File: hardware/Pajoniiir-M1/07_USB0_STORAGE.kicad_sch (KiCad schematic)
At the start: 7 parts

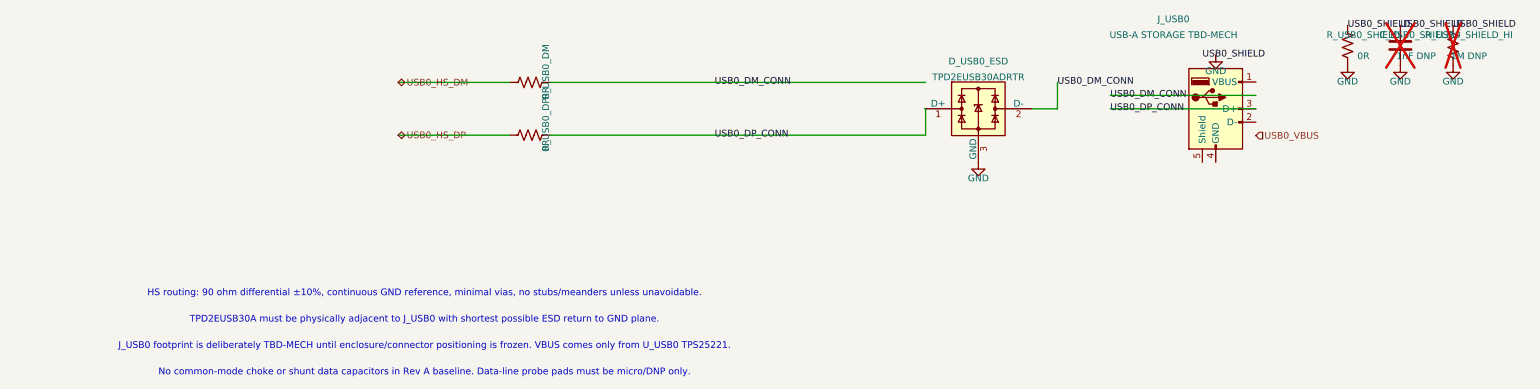
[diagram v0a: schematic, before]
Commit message: hardware: snap child sheets 06-10 to 25 mil grid
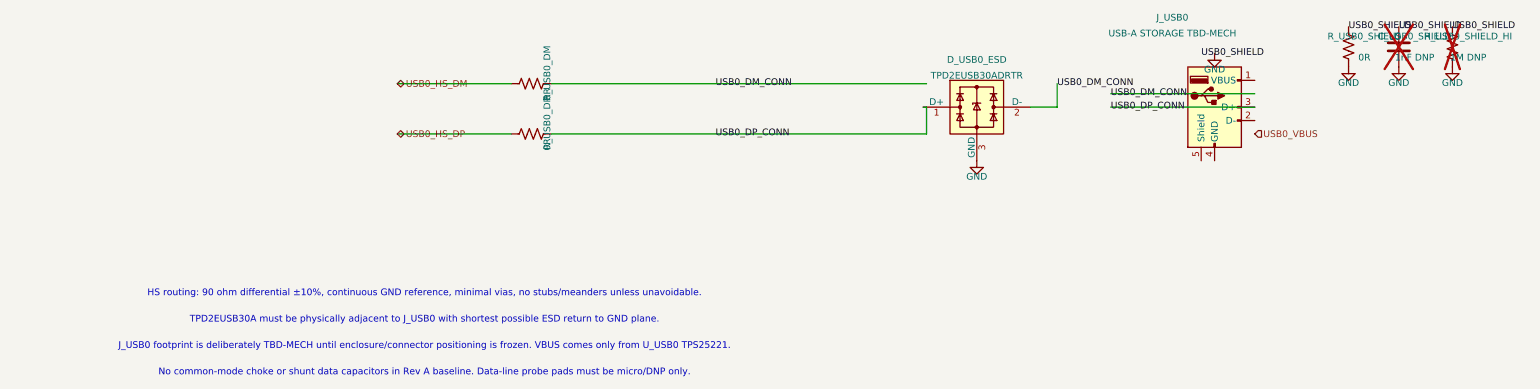
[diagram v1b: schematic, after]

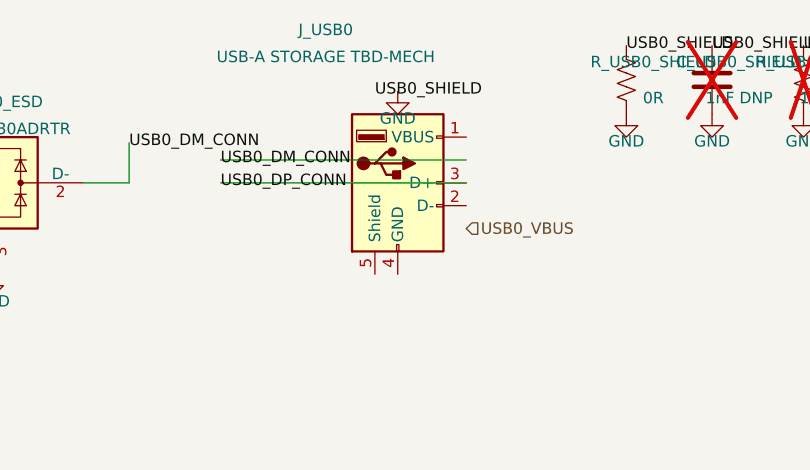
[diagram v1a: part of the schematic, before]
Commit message: hardware: correct USB-A connector pin mapping
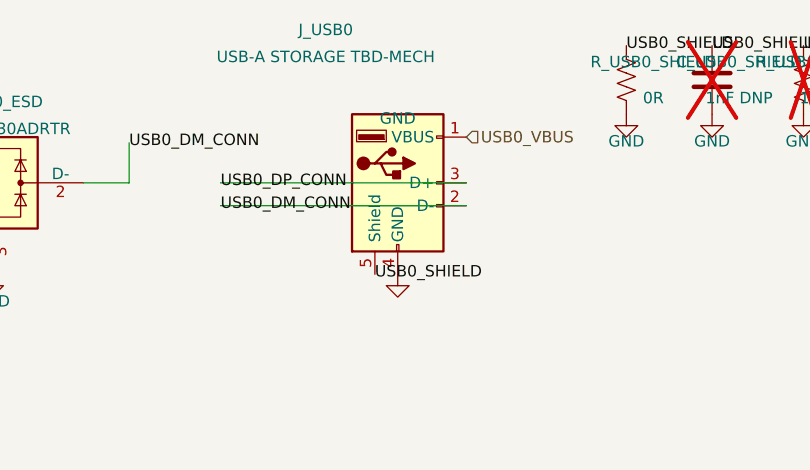
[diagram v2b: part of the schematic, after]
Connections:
- net GND: now also J_USB0.4 (GND)
- net USB0_DM_CONN: now also J_USB0.2 (D-)
- net USB0_SHIELD: now also J_USB0.5 (Shield)
- net USB0_VBUS: now also J_USB0.1 (VBUS)
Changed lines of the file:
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@@
     (instances (project "Pajoniiir-M1" (path "/2c8dd352-b7b8-4d9e-8f93-5dd43be2a100/31000007-6b2a-4a3a-8c91-000000000007" (reference "J_USB0") (unit 1))))
   )
-  (hierarchical_label "USB0_VBUS" (shape input) (at 192.405 64.77 0) (effects (font (size 1.27 1.27))))
-  (wire (pts (xy 192.405 57.15) (xy 165.1 57.15)) (stroke (width 0) (type default)))
-  (label "USB0_DM_CONN" (at 165.1 57.15 0) (effects (font (size 1.27 1.27))))
+  (hierarchical_label "USB0_VBUS" (shape input) (at 192.405 54.61 0) (effects (font (size 1.27 1.27))))
+  (wire (pts (xy 192.405 62.23) (xy 165.1 62.23)) (stroke (width 0) (type default)))
+  (label "USB0_DM_CONN" (at 165.1 62.23 0) (effects (font (size 1.27 1.27))))
   (wire (pts (xy 192.405 59.69) (xy 165.1 59.69)) (stroke (width 0) (type default)))
   (label "USB0_DP_CONN" (at 165.1 59.69 0) (effects (font (size 1.27 1.27))))
   (symbol
-    (lib_id "power:GND") (at 184.785 49.53 0) (unit 1)
+    (lib_id "power:GND") (at 184.785 69.85 0) (unit 1)
     (exclude_from_sim no) (in_bom yes) (on_board yes) (dnp no)
     (property "Reference" "#PWR0702" (at 184.785 55.53 0) (effects (font (size 1.27 1.27)) (hide yes)))
@@
     (instances (project "Pajoniiir-M1" (path "/2c8dd352-b7b8-4d9e-8f93-5dd43be2a100/31000007-6b2a-4a3a-8c91-000000000007" (reference "#PWR0702") (unit 1))))
   )
-  (label "USB0_SHIELD" (at 182.245 49.53 0) (effects (font (size 1.27 1.27))))
+  (label "USB0_SHIELD" (at 182.245 69.85 0) (effects (font (size 1.27 1.27))))
   (symbol
     (lib_id "Device:R_US") (at 210.185 48.26 0) (unit 1)

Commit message: hardware: declare verified rail power sources for ERC
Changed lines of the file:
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@@
   (text "J_USB0 footprint is deliberately TBD-MECH until enclosure/connector positioning is frozen. VBUS comes only from U_USB0 TPS25221." (exclude_from_sim no) (at 35 105 0) (effects (font (size 1.27 1.27))))
   (text "No common-mode choke or shunt data capacitors in Rev A baseline. Data-line probe pads must be micro/DNP only." (exclude_from_sim no) (at 35 110 0) (effects (font (size 1.27 1.27))))
+  (symbol
+    (lib_id "power:PWR_FLAG")
+    (at 192.405 54.61 0)
+    (unit 1)
+    (exclude_from_sim no)
+    (in_bom yes)
+    (on_board yes)
+    (dnp no)
+    (property "Reference" "#FLG0701" (at 192.405 56.515 0) (effects (font (size 1.27 1.27)) (hide yes)))
+    (property "Value" "PWR_FLAG" (at 192.405 58.42 0) (effects (font (size 1.27 1.27))))
+    (property "Footprint" "" (at 192.405 54.61 0) (effects (font (size 1.27 1.27)) (hide yes)))
+    (property "Datasheet" "~" (at 192.405 54.61 0) (effects (font (size 1.27 1.27)) (hide yes)))
+    (property "Description" "Special symbol for telling ERC where power comes from" (at 192.405 54.61 0) (effects (font (size 1.27 1.27)) (hide yes)))
+    (pin "1")
+    (instances (project "Pajoniiir-M1" (path "/2c8dd352-b7b8-4d9e-8f93-5dd43be2a100/31000007-6b2a-4a3a-8c91-000000000007" (reference "#FLG0701") (unit 1))))
+  )
   (sheet_instances (path "/" (page "8")))
   (embedded_fonts no)
